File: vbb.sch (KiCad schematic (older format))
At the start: 16 parts, among them CON1 BARREL_JACK, J1 Screw_Terminal_1x02, J2 XM7D-0512, P1 CONN_02X01, P2 CONN_02X03, P3 CONN_02X04, P4 USB_B, P5 CONN_02X03, P6 USB_B, P7 USB_A, P8 CONN_02X03, P9 CONN_02X03

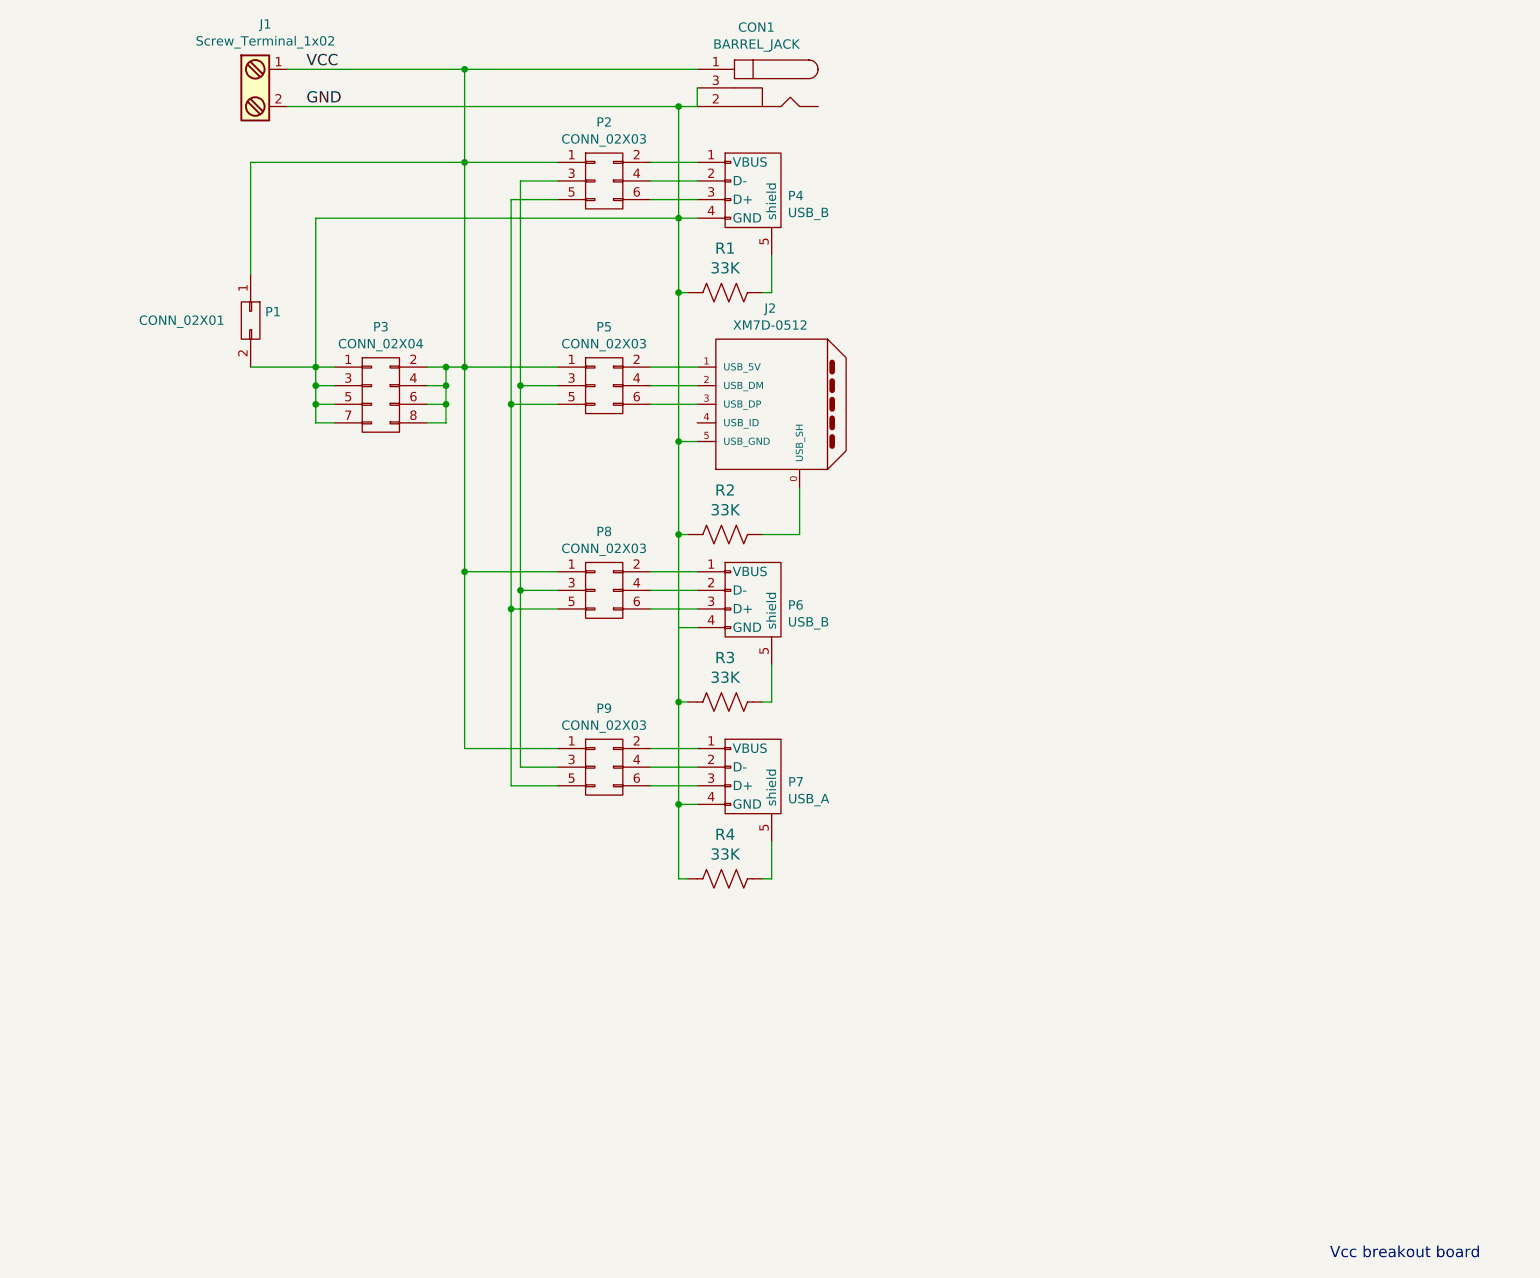
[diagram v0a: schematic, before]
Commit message: Files should be ready: Copper pours on both sides Added jumpers for current measurement Added silkscreen text VCC/GNC tracks are twice as wide.
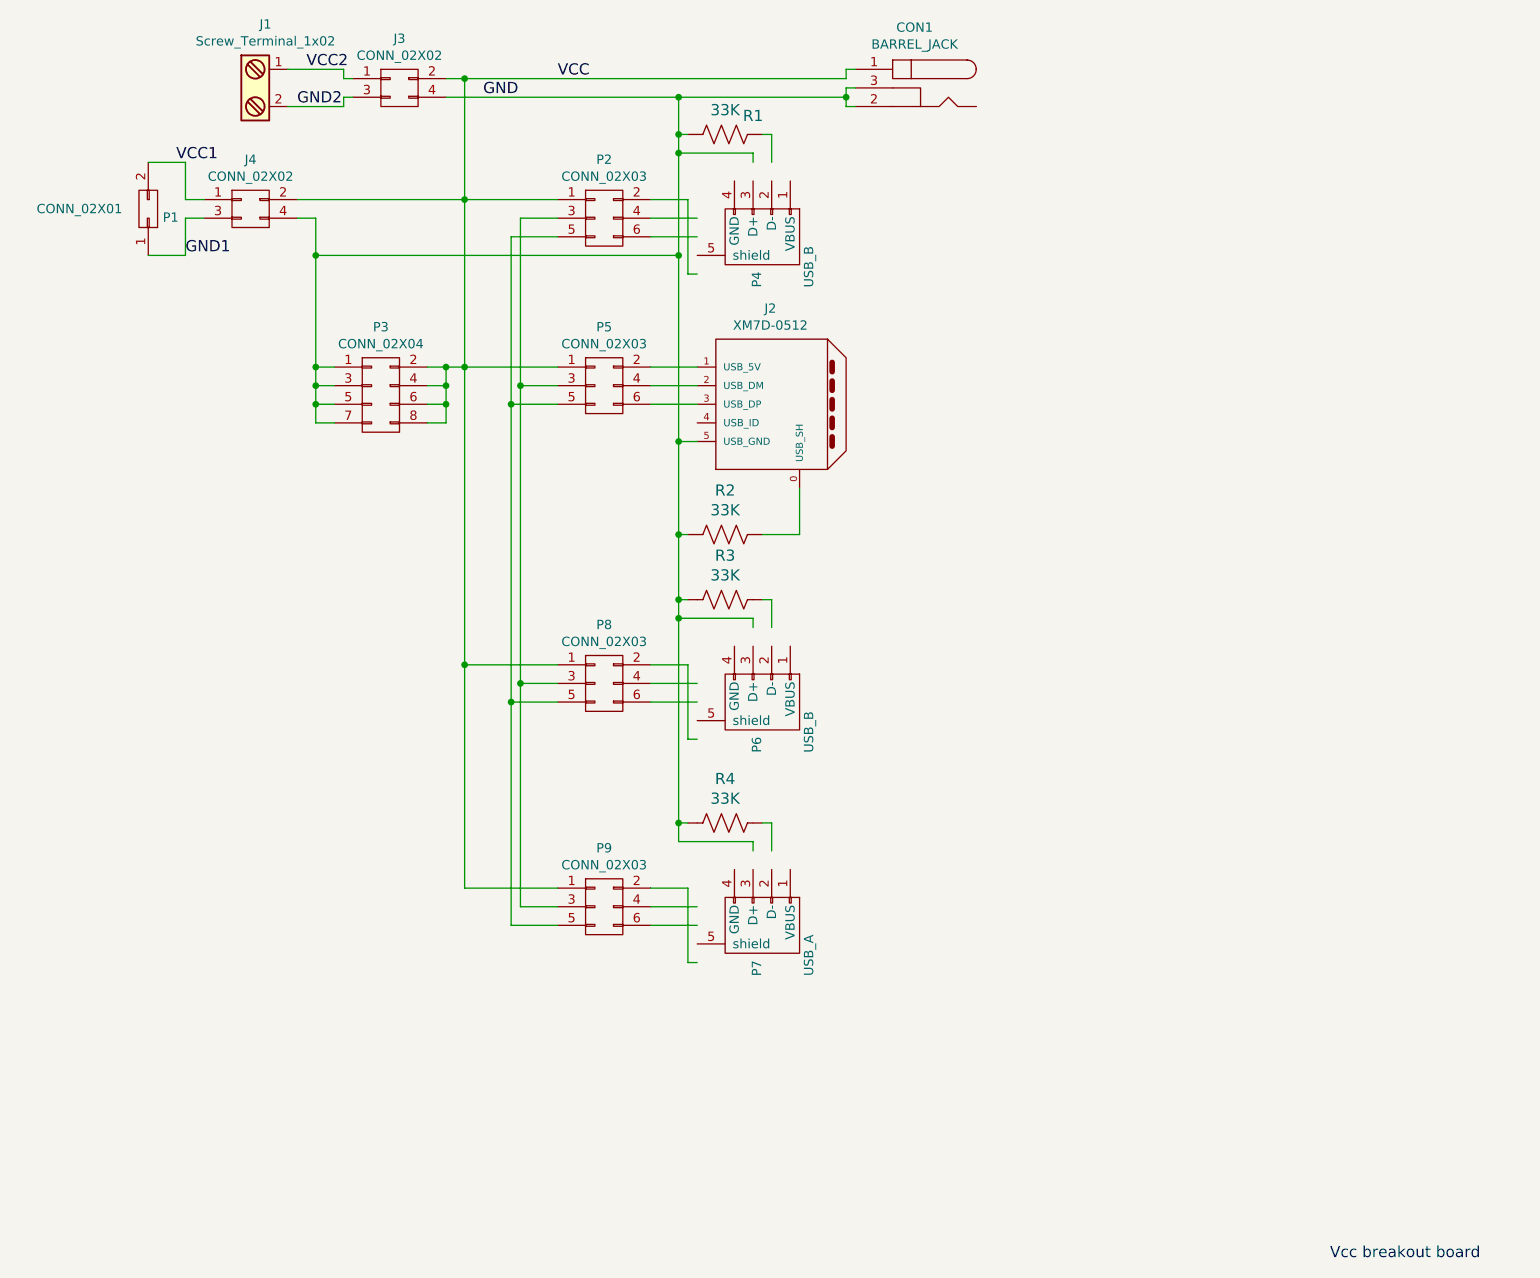
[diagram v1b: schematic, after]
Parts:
- added J3, J4: CONN_02X02, Pin_Headers:Pin_Header_Straight_2x02_Pitch2.54mm, symbol CONN_02X02
- P2, P5, P8, P9: footprint Pin_Headers:Pin_Header_Straight_2x03 -> Pin_Headers:Pin_Header_Straight_2x03_Pitch2.54mm
- P3: footprint Pin_Headers:Pin_Header_Straight_2x04 -> Pin_Headers:Pin_Header_Straight_2x04_Pitch2.54mm
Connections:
- net labels added: GND1, GND2, VCC1, VCC2
- wire segments 57 -> 83
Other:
- moved on the sheet: CON1, P1, P2, P4, P6, P7, P8, P9, R1, R3, R4

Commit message: Final (?) files. Swapped Banana jack pins on both PCB and schematics to have Red VCC, Black GND rendering. No actual layout change. Rearranged references on board Added VCC/GND marks on back side.
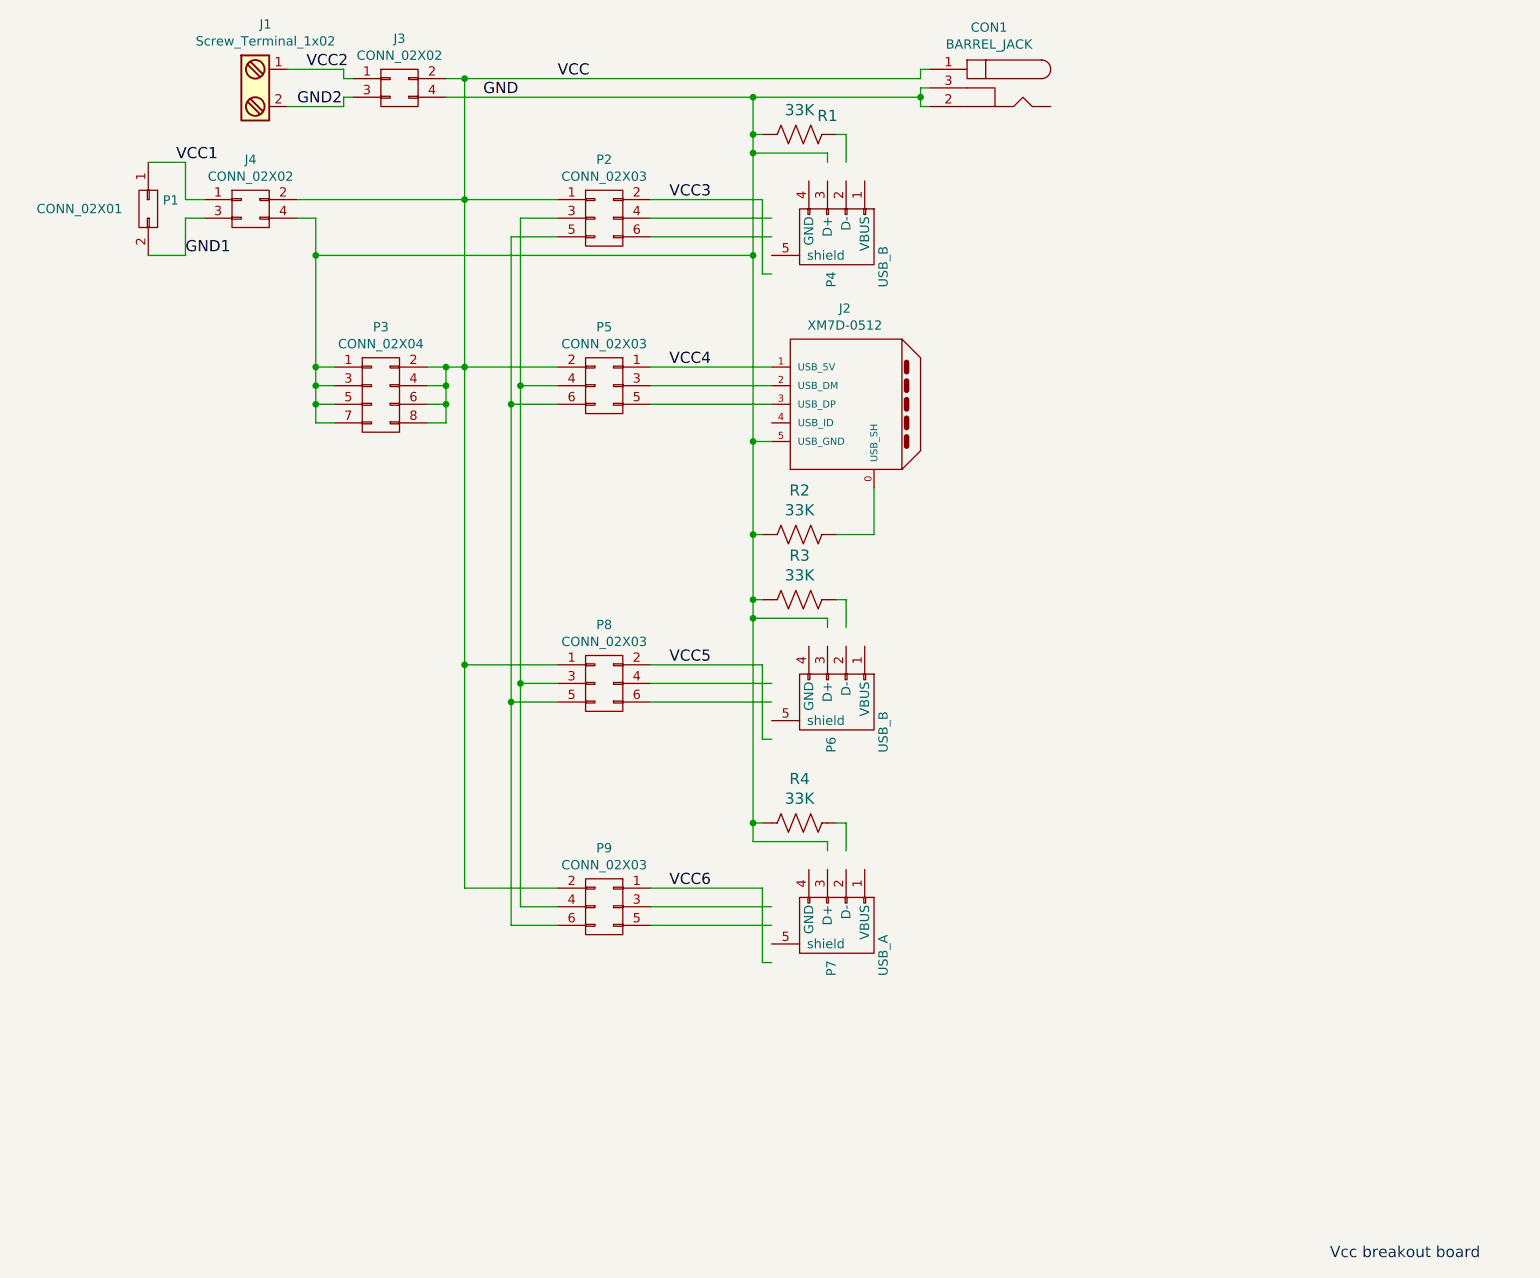
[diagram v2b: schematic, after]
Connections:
- net labels added: VCC3, VCC4, VCC5, VCC6
- wire segments 83 -> 110
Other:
- moved on the sheet: CON1, J2, P4, P6, P7, R1, R2, R3, R4

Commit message: Is this the final one? I think I haven't saved the schematics
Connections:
- wire segments 110 -> 83
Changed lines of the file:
@@
 Connection ~ 4350 3100
 Wire Wire Line
-	1900 1800 2800 1800
+	1900 1800 3300 1800
 Wire Wire Line
-	2800 1800 3300 1800
-Wire Wire Line
-	2800 1150 2800 1800
-Wire Wire Line
-	2800 1800 2800 2700
-Wire Wire Line
-	2800 2700 2800 4300
-Wire Wire Line
-	2800 4300 2800 5500
+	2800 1150 2800 5500
 Connection ~ 2800 1150
 Wire Wire Line
-	2600 2700 2700 2700
-Wire Wire Line
-	2700 2700 2800 2700
-Wire Wire Line
-	2800 2700 3300 2700
+	2600 2700 3300 2700
 Connection ~ 2800 1800
 Wire Wire Line
@@
 	2800 4300 3300 4300
 Wire Wire Line
-	2700 2700 2700 2800
-Wire Wire Line
-	2700 2800 2700 2900
-Wire Wire Line
-	2700 2900 2700 3000
+	2700 2700 2700 3000
 Wire Wire Line
 	2700 2800 2600 2800
@@
 Connection ~ 2700 2900
 Wire Wire Line
-	2000 1900 2000 2100
-Wire Wire Line
-	2000 2100 2000 2700
-Wire Wire Line
-	2000 2700 2000 2800
-Wire Wire Line
-	2000 2800 2000 2900
-Wire Wire Line
-	2000 2900 2000 3000
+	2000 1900 2000 3000
 Wire Wire Line
 	2000 2800 2100 2800
@@
 	3050 5700 3300 5700
 Wire Wire Line
-	3050 2000 3050 2900
-Wire Wire Line
-	3050 2900 3050 4500
-Wire Wire Line
-	3050 4500 3050 5700
+	3050 2000 3050 5700
 Wire Wire Line
 	3050 4500 3300 4500
@@
 	3100 5600 3300 5600
 Wire Wire Line
-	3100 1900 3100 2800
-Wire Wire Line
-	3100 2800 3100 4400
-Wire Wire Line
-	3100 4400 3100 5600
+	3100 1900 3100 5600
 Wire Wire Line
 	3100 4400 3300 4400
@@
 	5000 3600 5000 3350
 Wire Wire Line
-	4350 1250 4350 1450
-Wire Wire Line
-	4350 1450 4350 1550
-Wire Wire Line
-	4350 1550 4350 2100
-Wire Wire Line
-	4350 2100 4350 3100
-Wire Wire Line
-	4350 3100 4350 3600
-Wire Wire Line
-	4350 3600 4350 3950
-Wire Wire Line
-	4350 3950 4350 4050
-Wire Wire Line
-	4350 4050 4350 5150
-Wire Wire Line
-	4350 5150 4350 5250
+	4350 1250 4350 5250
 Connection ~ 3100 4400
 Connection ~ 3050 4500
@@
 	4850 1450 4850 1600
 Wire Wire Line
-	2700 1250 4350 1250
+	2700 1250 5250 1250
 Wire Wire Line
-	4350 1250 5250 1250
-Wire Wire Line
-	2700 1150 2800 1150
-Wire Wire Line
-	2800 1150 5250 1150
+	2700 1150 5250 1150
 Wire Wire Line
 	2200 1150 2150 1150
@@
 	5250 1100 5300 1100
 Wire Wire Line
-	5250 1200 5250 1250
-Wire Wire Line
-	5250 1250 5250 1300
+	5250 1200 5250 1300
 Wire Wire Line
 	5250 1200 5300 1200

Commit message: Files as delivered for manufacturing.
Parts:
- removed P1: CONN_02X01, Connect:Banana_Jack_2Pin, symbol CONN_02X01
- added J5, J6: CONN_01X01, Connectors:Banana_Jack_1Pin, symbol CONN_01X01
- added P1: USB_A, udif:MOLEX-48037-0001, symbol USB_A
- J2: value XM7D-0512 -> Mini-B
- P6: value USB_B -> Micro_B
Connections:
- wire segments 83 -> 93
